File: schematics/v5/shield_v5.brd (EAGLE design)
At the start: 41 x 50 mm, 47 parts, among them IC1 L293DD, IC2 74HCT04D, Q2 PMV20EN, Q3 PMV20EN, Q4 PMV20EN, Q5 PMV20EN, U1 ATMEGA168

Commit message: updated routing
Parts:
- moved SJ2 2.18 mm to (7.82, 25.2)
- moved C2 1.97 mm to (7.95, 28.3)
- moved R1 1.82 mm to (11.4, 24.7)
- moved JP2 1.62 mm to (15.3, 19.9)
- moved R4 1.29 mm to (15.2, 15.3)
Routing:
- net N$1: track 39.4 -> 32.9 mm, vias 4 -> 2
- net GND: track 243.0 -> 246.4 mm
- net P2: track 23.8 -> 26.7 mm
- net OC2_PWM2: track 46.6 -> 44.5 mm
- net IN1: track 36.4 -> 38.5 mm
- net VCC: track 100.3 -> 98.5 mm
- net RESET: track 38.9 -> 37.2 mm
- net OC0_PWM2: track 32.1 -> 33.6 mm
- net N$10: track 19.5 -> 18.7 mm
- net TX_PC: track 27.2 -> 26.5 mm
- net N$23: track 7.71 -> 8.24 mm
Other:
- board text added: "C.H.I.P. DIP v2.2 LED Motor JKW"
- board text removed: "C.H.I.P. DIP v2.2 LED/Motor JKW"

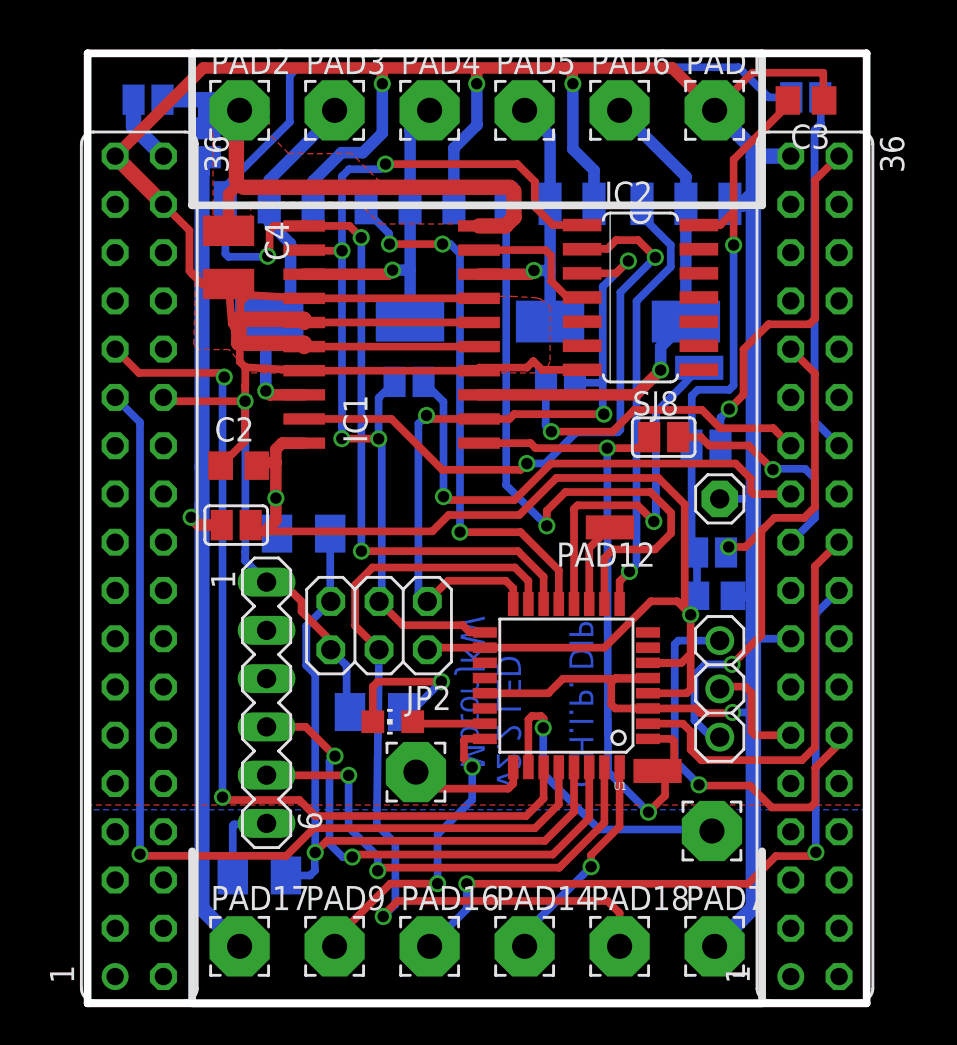
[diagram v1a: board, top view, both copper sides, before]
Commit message: rerouting to fix osh DRU issues
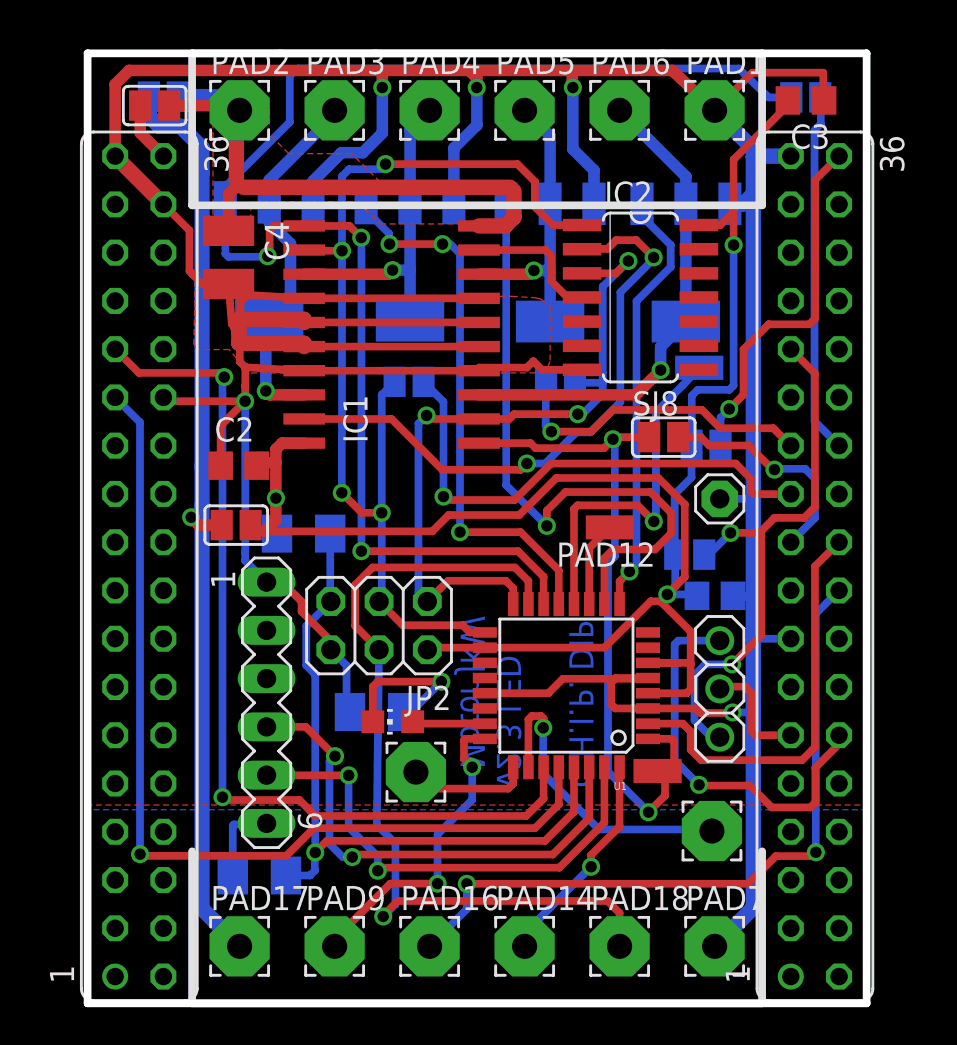
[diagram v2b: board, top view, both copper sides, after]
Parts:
- moved SJ5 3.29 mm to (3.99, 47.7), turned to 180 degrees
- moved SJ4 1.16 mm to (31.7, 23.6)
- moved SJ1 0.47 mm to (3.53, 47.2), flipped to the top, turned to 0 degrees
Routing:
- net VIN2: track 45.2 -> 50.2 mm
- net IN3: track 51.0 -> 54.4 mm
- net GND: track 246.4 -> 248.6 mm
- net VIN: track 30.6 -> 32.1 mm
- net 3V3: track 28.5 -> 29.7 mm
- net N$1: track 32.9 -> 31.9 mm
- net IN1: track 38.5 -> 37.7 mm
- net OC2_PWM1: track 35.5 -> 36.2 mm
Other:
- board text added: "C.H.I.P. DIP v2.3 LED Motor JKW"
- board text removed: "C.H.I.P. DIP v2.2 LED Motor JKW"

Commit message: cleaned schematics
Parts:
- removed R2: (no value), rcl:M1206
- added C12: (no value), rcl:C1206
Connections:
- net N$10 renamed PB0
- net N$13 renamed PD2
- net N$15 renamed PC1
- net N$16 renamed PC2
- net N$17 renamed PC3
- net N$2 renamed UNCONNECTED_GND
- net N$4 renamed PD7
- new net D0: SV3.5
- net N$9: now also C12.2; no longer R2.2
- net RESET: now also C12.1; no longer R2.1
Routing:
- net GND: track 248.6 -> 249.1 mm
- net VIN: track 32.1 -> 31.6 mm
